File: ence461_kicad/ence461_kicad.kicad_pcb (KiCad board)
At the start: 2 copper layers, 58 x 30 mm, 98 parts, among them J1 SWD, J2 INPUT_0, J3 INPUT_1, J4 CANBUS, J5 INPUT_2, J6 POWER, Q1 Q_PMOS_GSD, U1 LMV324, U2 LMV324, U3 LMV324, U4 74HC3G14DP, U5 LMV321, U6 NCV7344D13R2GOSCT-ND, U7 MIC5202, U9 MKE16Z32VLD4

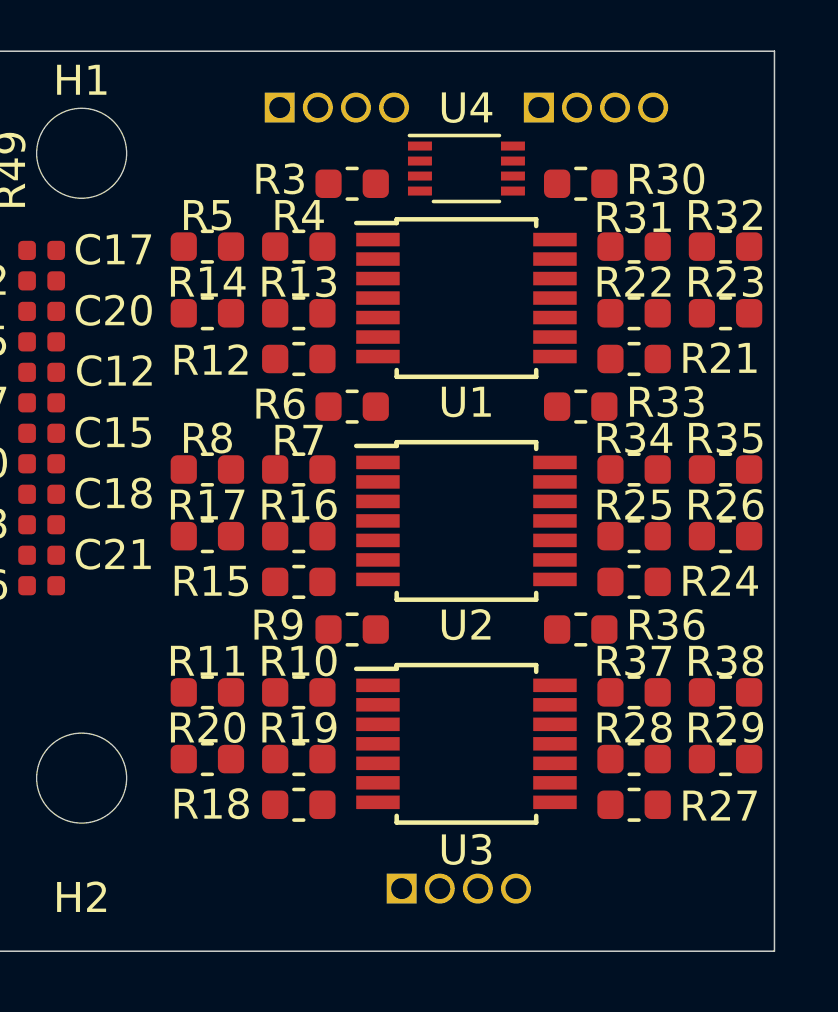
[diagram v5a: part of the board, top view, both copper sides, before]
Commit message: Added a model for the power connector.
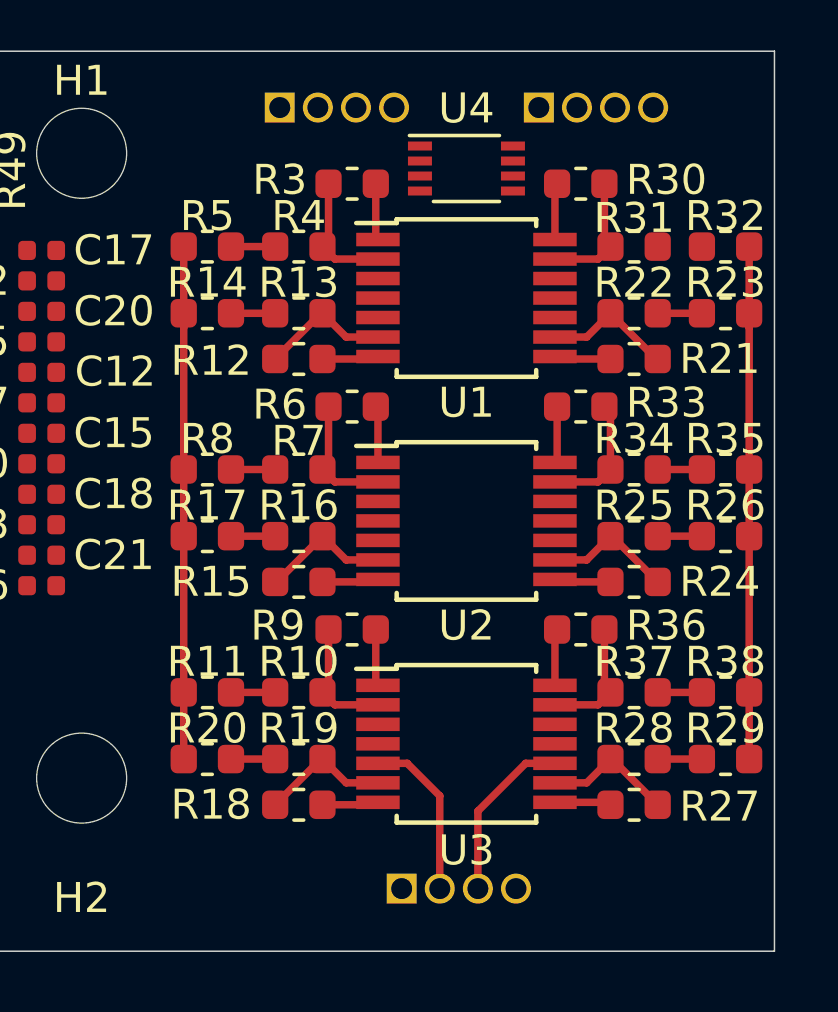
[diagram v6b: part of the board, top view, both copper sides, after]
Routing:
- net +2V5: track 0.00 -> 34.2 mm
- net /CURRENT_10: track 0.00 -> 5.81 mm
- net /CURRENT_09: track 0.00 -> 5.60 mm
- net Net-(R27-Pad2): track 0.00 -> 4.38 mm
- net Net-(R24-Pad2): track 0.00 -> 4.38 mm
- net Net-(R21-Pad2): track 0.00 -> 4.38 mm
- net Net-(R18-Pad2): track 0.00 -> 4.38 mm
- net Net-(R15-Pad2): track 0.00 -> 4.38 mm
- net Net-(R12-Pad2): track 0.00 -> 4.38 mm
- net Net-(R33-Pad2): track 0.00 -> 4.20 mm
- net Net-(R36-Pad2): track 0.00 -> 4.20 mm
- net Net-(R30-Pad2): track 0.00 -> 4.20 mm
- net Net-(R6-Pad2): track 0.00 -> 4.20 mm
- net Net-(R3-Pad2): track 0.00 -> 4.20 mm
- net Net-(R10-Pad2): track 0.00 -> 4.20 mm
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
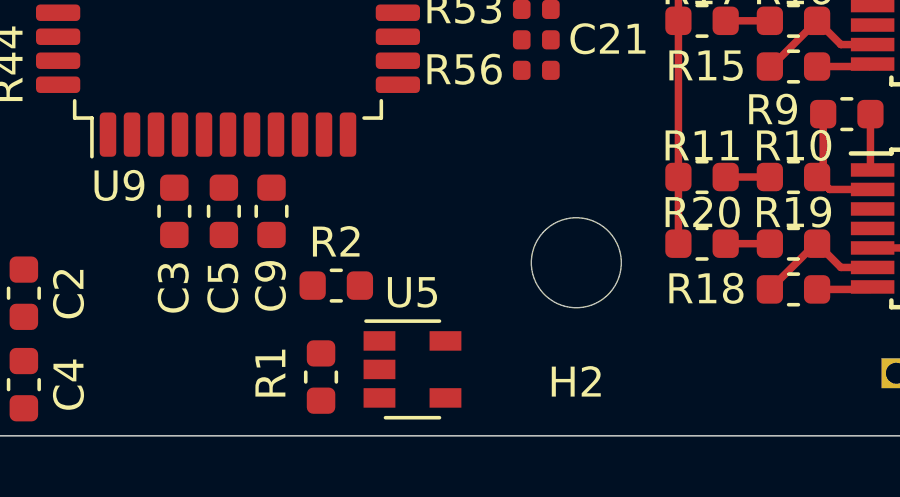
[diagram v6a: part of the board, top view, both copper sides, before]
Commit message: Added schematics for diagrams. Fixed virtual ground mistake.
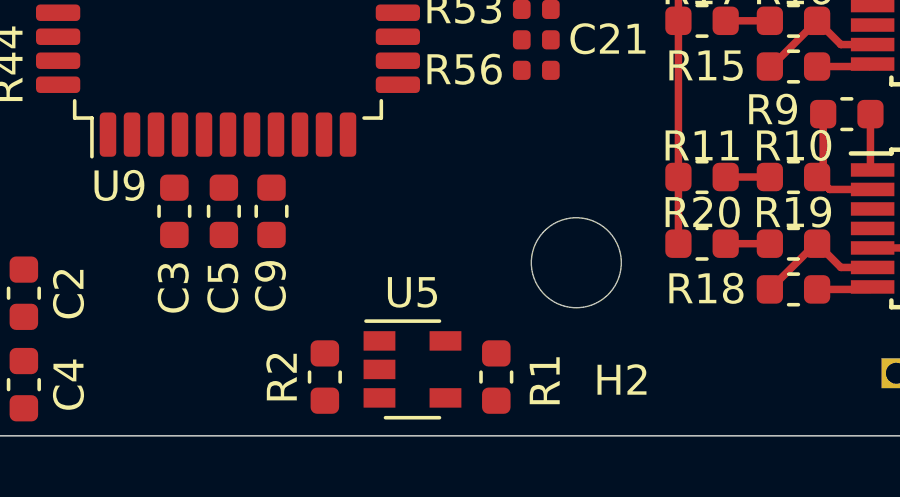
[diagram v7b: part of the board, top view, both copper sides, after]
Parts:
- R10, R13, R16, R19, R22, R25, R28, R31, R34, R37, R4, R7: value 920 R -> 1 K
- R11, R14, R17, R20, R23, R26, R29, R32, R35, R38, R5, R8: value 8.2 R -> 10 R
- R12, R15, R18, R21, R24, R27, R3, R30, R33, R36, R6, R9: value 130 K -> 100 K
- moved R1 5.84 mm to (134.2, 66.0), turned to 270 degrees
- moved R2 3.07 mm to (128.5, 66.0), turned to 270 degrees
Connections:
- U5 pad 2: /VCC_OPAMP -> GND
- U5 pad 5: GND -> /VCC_OPAMP
